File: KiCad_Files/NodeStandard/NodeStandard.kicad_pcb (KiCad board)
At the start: 2 copper layers, 129 x 160.4 mm, 111 parts, among them J1 AC Current In, J10 Opto Coupler 1 in, J11 Opto Coupler 2 in, J12 Opto Coupler 3 in, J13 Relay 1 Output, J14 Relay 2 Output, J15 Switch 3 in, J16 Switch 2 in, J17 Switch 1 in, J18 Force output FET 1 on, J19 Force output FET 2 on, J2 Current coil in, J20 FET 1 Output, J21 FET 2 Output, J22 Force output Relay 3 on, J23 Relay 3 Output 1, J24 Relay 3 Output 2, J25 230VAC in, J26 5V-in, J27 ExtDC-in, J28 Hal current sensor, J29 Current sensor select, J3 AC Current loop, J4 EXT1, J5 OledDisplay, J6 RFIDReader, J7 EXT2, J8 Force output Relay 1 on, J9 Force output Relay 2 on, K1 SANYOU_SRD_Form_C, K2 SANYOU_SRD_Form_C, K3 RT42xAxx, Q1 BC547, Q2 BC547, Q3 IRLZ34N, Q4 IRLZ34N, Q5 BC547, U1 MCP23017_SP

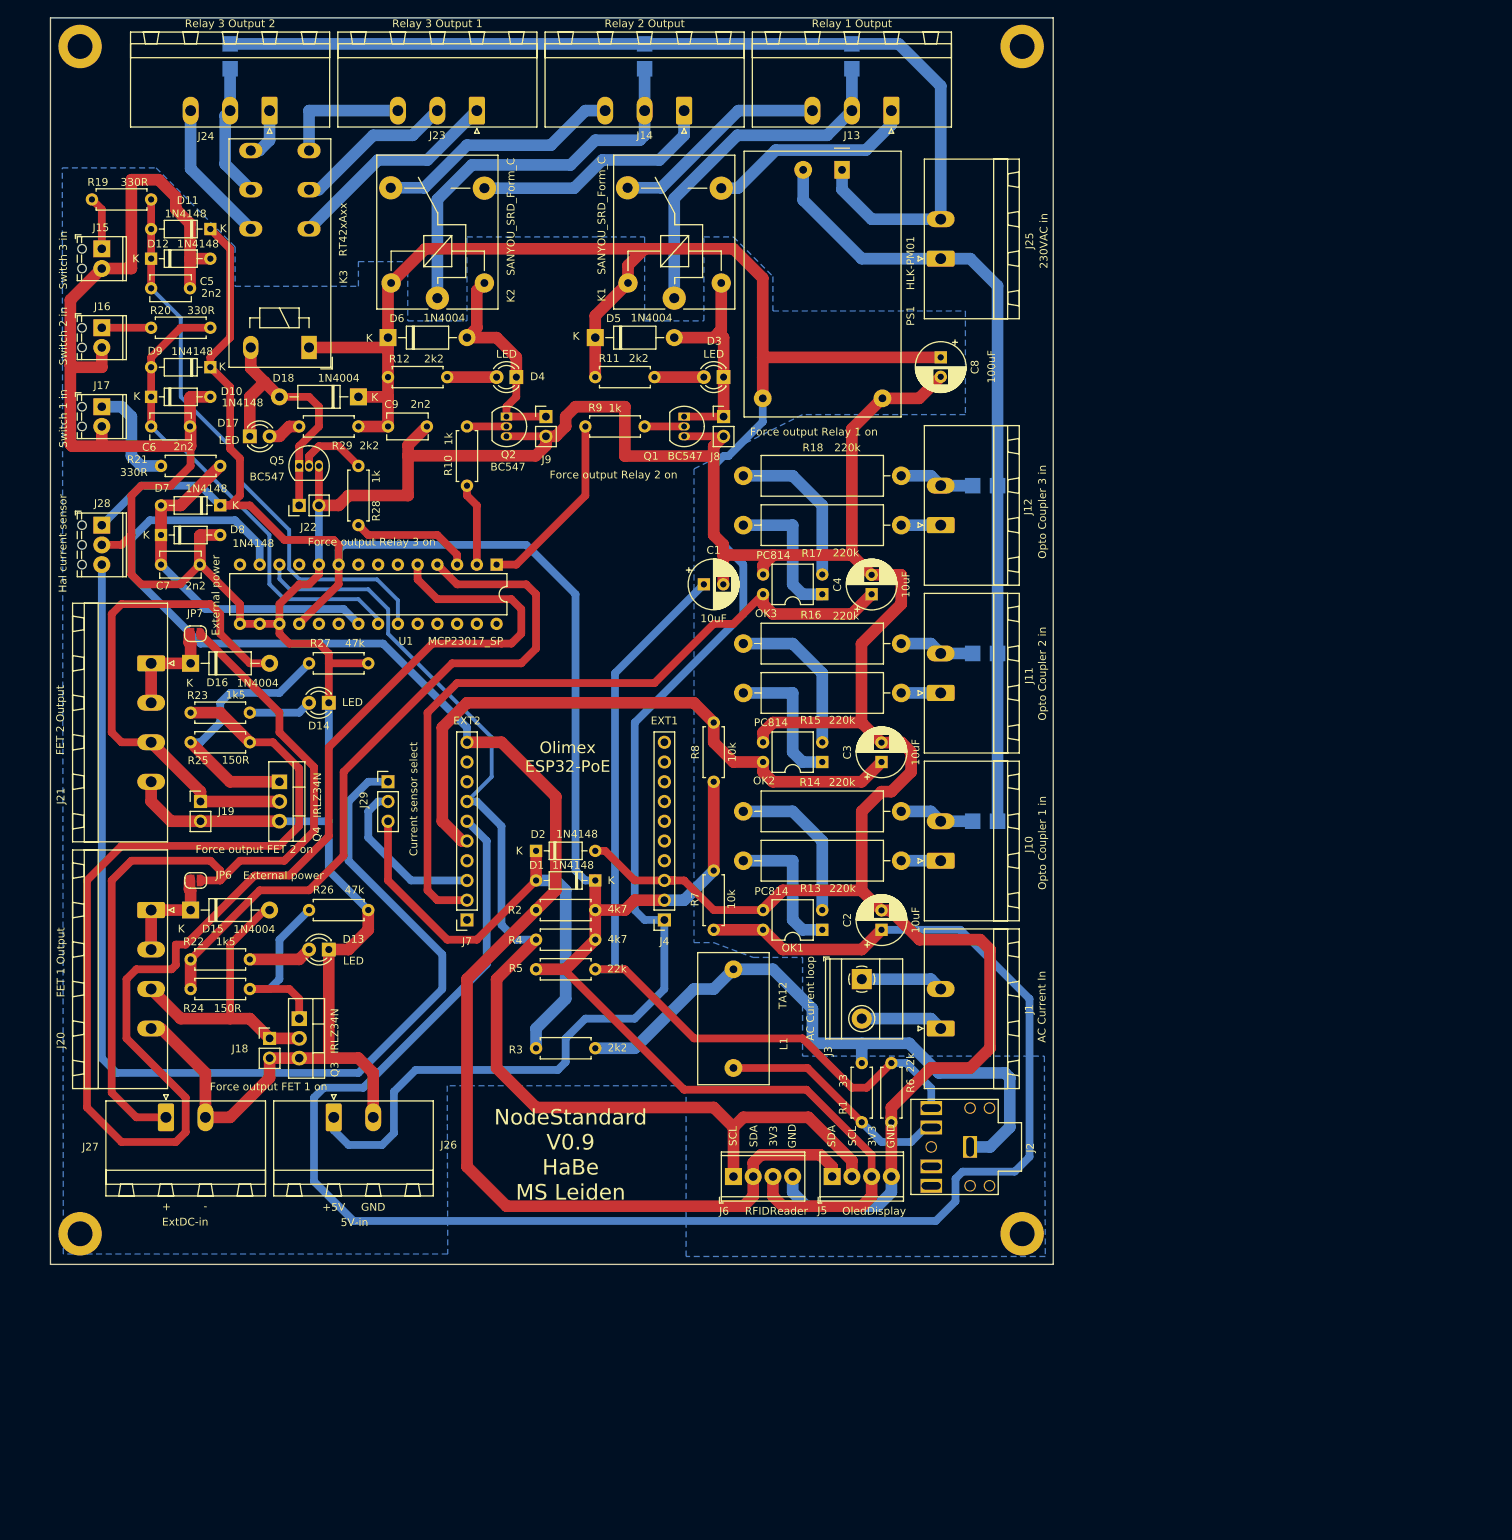
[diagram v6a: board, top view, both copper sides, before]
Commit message: Version 0.9 corrected typo's on silk screen added ESP32 model on silk screen + added 2 holes to fixate ESP32 with tie wrap or so
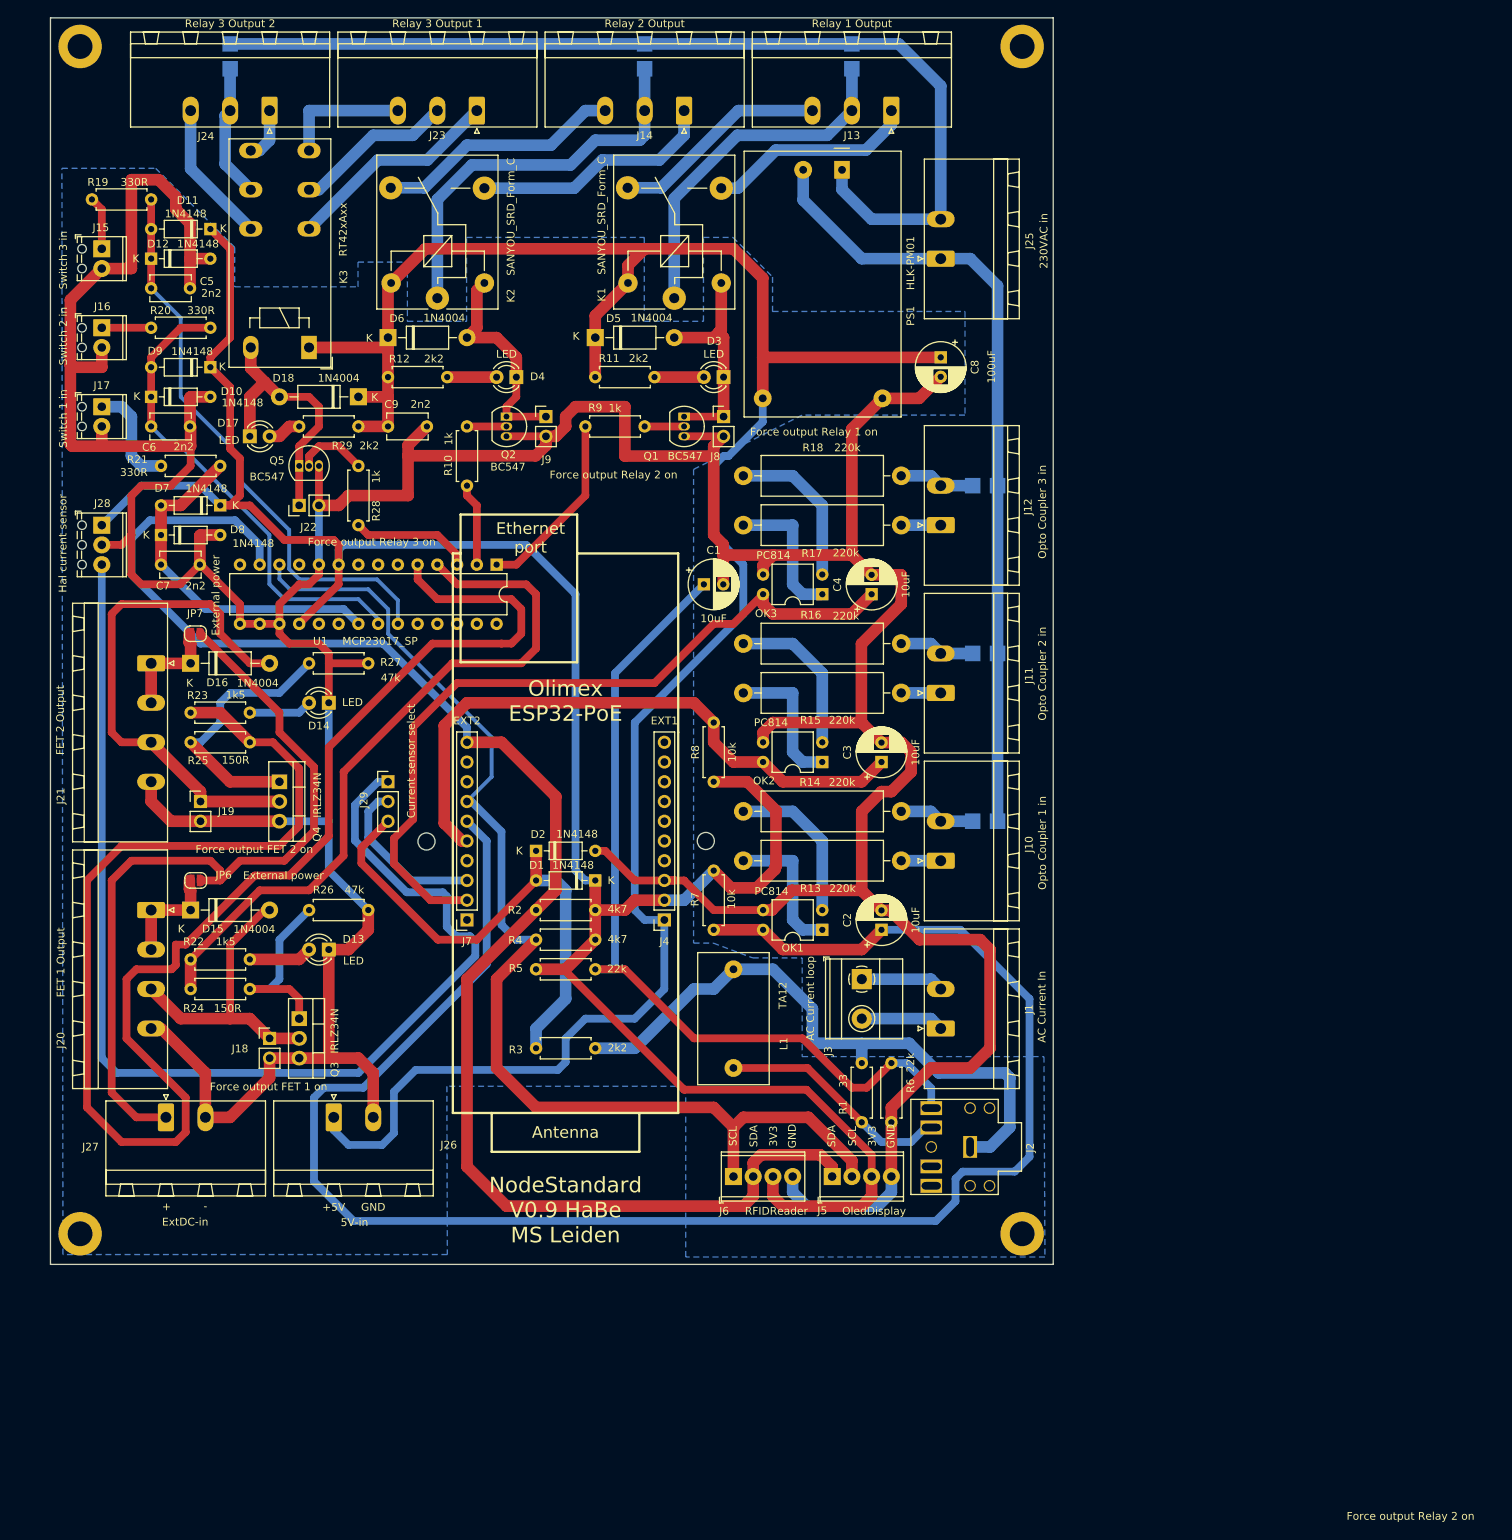
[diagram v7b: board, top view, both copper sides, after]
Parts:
- added ?: , , F.Cu at (91.0, 87.0)
- added REF**: MountingHole_2.2mm_M2_DIN965, MountingHole:MountingHole_2.2mm_M2_DIN965, F.Cu at (114.6, 127.0)
- added REF**: MountingHole_2.2mm_M2_DIN965, MountingHole:MountingHole_2.2mm_M2_DIN965, F.Cu at (78.6, 127.1)
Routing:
- net +3V3: track 279.6 -> 295.1 mm
- net Net-(J28-Pad3): track 147.8 -> 153.7 mm
- net GPI36_U1RXD: track 94.8 -> 98.9 mm
- net Net-(D1-Pad2): track 63.0 -> 66.6 mm
- net GPIO33: track 81.6 -> 80.7 mm
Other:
- board text added: "Antenna"
- board text added: "Ethernet port"

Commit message: V0.0.9.0 added a number of improvements
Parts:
- removed ?: , 
- added LM2596IN+1: IN+, TestPoint:TestPoint_THTPad_2.0x2.0mm_Drill1.0mm, F.Cu at (134.1, 44.8)
- added LM2596IN-1: IN-, TestPoint:TestPoint_THTPad_2.0x2.0mm_Drill1.0mm, F.Cu at (116.6, 44.8)
- added LM2596Out+1: Out+, TestPoint:TestPoint_THTPad_2.0x2.0mm_Drill1.0mm, F.Cu at (134.1, 84.8)
- added LM2596Out-1: OUT-, TestPoint:TestPoint_THTPad_2.0x2.0mm_Drill1.0mm, F.Cu at (116.7, 84.8)
- added Q6: 2N3906, Package_TO_SOT_THT:TO-92_Inline, F.Cu at (94.6, 126.4)
- added R30: 1k, Resistor_THT:R_Axial_DIN0207_L6.3mm_D2.5mm_P7.62mm_Horizontal, F.Cu at (88.3, 134.0)
- added REF**: TestPoint_THTPad_D2.0mm_Drill1.0mm, TestPoint:TestPoint_THTPad_D2.0mm_Drill1.0mm, F.Cu at (111.4, 172.4)
- added REF**: TestPoint_THTPad_D2.0mm_Drill1.0mm, TestPoint:TestPoint_THTPad_D2.0mm_Drill1.0mm, F.Cu at (111.4, 153.6)
- added TP5: La, TestPoint:TestPoint_THTPad_2.0x2.0mm_Drill1.0mm, F.Cu at (122.4, 170.4)
- added TP6: Lb, TestPoint:TestPoint_THTPad_2.0x2.0mm_Drill1.0mm, F.Cu at (122.4, 155.6)
- J25: value 230VAC in -> 230VAC/12-40VDC in
- moved L1 13.6 mm to (115.6, 163.2)
- moved D15 11.7 mm to (43.8, 146.7)
- moved J20 11.7 mm to (38.7, 146.7)
- moved Q4 11.7 mm to (55.2, 130.2)
- moved R26 11.7 mm to (59.1, 146.7)
- moved REF** 11.7 mm to (29.6, 188.3)
- moved J1 11.7 mm to (140.3, 161.9)
- moved J10 11.7 mm to (140.3, 140.3)
- moved J29 11.7 mm to (69.2, 130.2)
- moved J4 11.7 mm to (104.8, 148.0)
- moved J7 11.7 mm to (79.4, 148.0)
- moved R1 11.7 mm to (130.2, 166.4)
- moved R13 11.7 mm to (135.3, 140.3)
- moved R14 11.7 mm to (135.3, 134.0)
- moved R2 11.7 mm to (95.9, 146.7)
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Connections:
- J2 pad R: Net-(J2-PadR) -> (no net)
- J2 pad RN: Net-(J2-PadRN) -> (no net)
- J4 pad 10: GPIO5_SPI_C5 -> (no net)
- J4 pad 4: ESP_EN -> (no net)
- J4 pad 5: GPIO0 -> (no net)
- J4 pad 6: GPIO1_U0TXD -> (no net)
- J4 pad 7: GPIO2_HS2_DATA0 -> (no net)
- J4 pad 8: GPIO3_U0RXD -> (no net)
- J4 pad 9: GPIO4_U1TXD -> (no net)
- J5 pad 3: +3V3 -> Net-(J5-Pad3)
- J6 pad 3: +3V3 -> Net-(J5-Pad3)
- J7 pad 1: GPI39 -> (no net)
- J7 pad 4: GPI34_BUT1 -> (no net)
- J7 pad 9: GPIO14_HS2_CLK -> (no net)
- R2 pad 1: +3V3 -> Net-(J5-Pad3)
- R4 pad 1: +3V3 -> Net-(J5-Pad3)
- U1 pad 11: Net-(U1-Pad11) -> (no net)
- U1 pad 14: Net-(U1-Pad14) -> (no net)
- U1 pad 19: Net-(U1-Pad19) -> (no net)
- U1 pad 20: Net-(U1-Pad20) -> (no net)
- U1 pad 24: Net-(U1-Pad24) -> (no net)
- U1 pad 25: Net-(U1-Pad25) -> (no net)
- U1 pad 26: Net-(U1-Pad26) -> (no net)
- U1 pad 27: Net-(U1-Pad27) -> (no net)
- U1 pad 28: Net-(U1-Pad28) -> (no net)
- U1 pad 6: Net-(U1-Pad6) -> (no net)
- U1 pad 7: Net-(U1-Pad7) -> (no net)
- U1 pad 8: Net-(U1-Pad8) -> (no net)
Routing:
- net Net-(J5-Pad3): track 0.00 -> 127.7 mm
- net +3V3: track 295.1 -> 224.4 mm
- net GND: track 661.1 -> 598.0 mm
- net +5V: track 292.8 -> 332.7 mm
- net 230VAC-N: track 102.4 -> 113.0 mm
- net GPIO15_HS2_CMD: track 0.00 -> 10.5 mm
- net Relay3: track 15.5 -> 25.7 mm
- net Relay2: track 10.7 -> 20.8 mm
- net Net-(J28-Pad3): track 153.7 -> 144.0 mm
- net Relay1: track 24.0 -> 32.7 mm
- net Net-(Q6-Pad2): track 0.00 -> 7.62 mm
- net 230VAC-L: track 127.6 -> 134.1 mm
- net Net-(J14-Pad2): track 51.3 -> 56.9 mm
- net Net-(J23-Pad1): track 27.9 -> 33.1 mm
- net GPIO32: track 225.6 -> 229.3 mm
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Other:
- board size 129 x 160.4 mm -> 129 x 170.6 mm
- board text added: "DC"
